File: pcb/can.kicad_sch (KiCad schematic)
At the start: 27 parts, among them J3 C-OBD-II-16M, J4 GND_Connect, U6 TCAN337, U7 LM2842X, U8 LM66100DCK

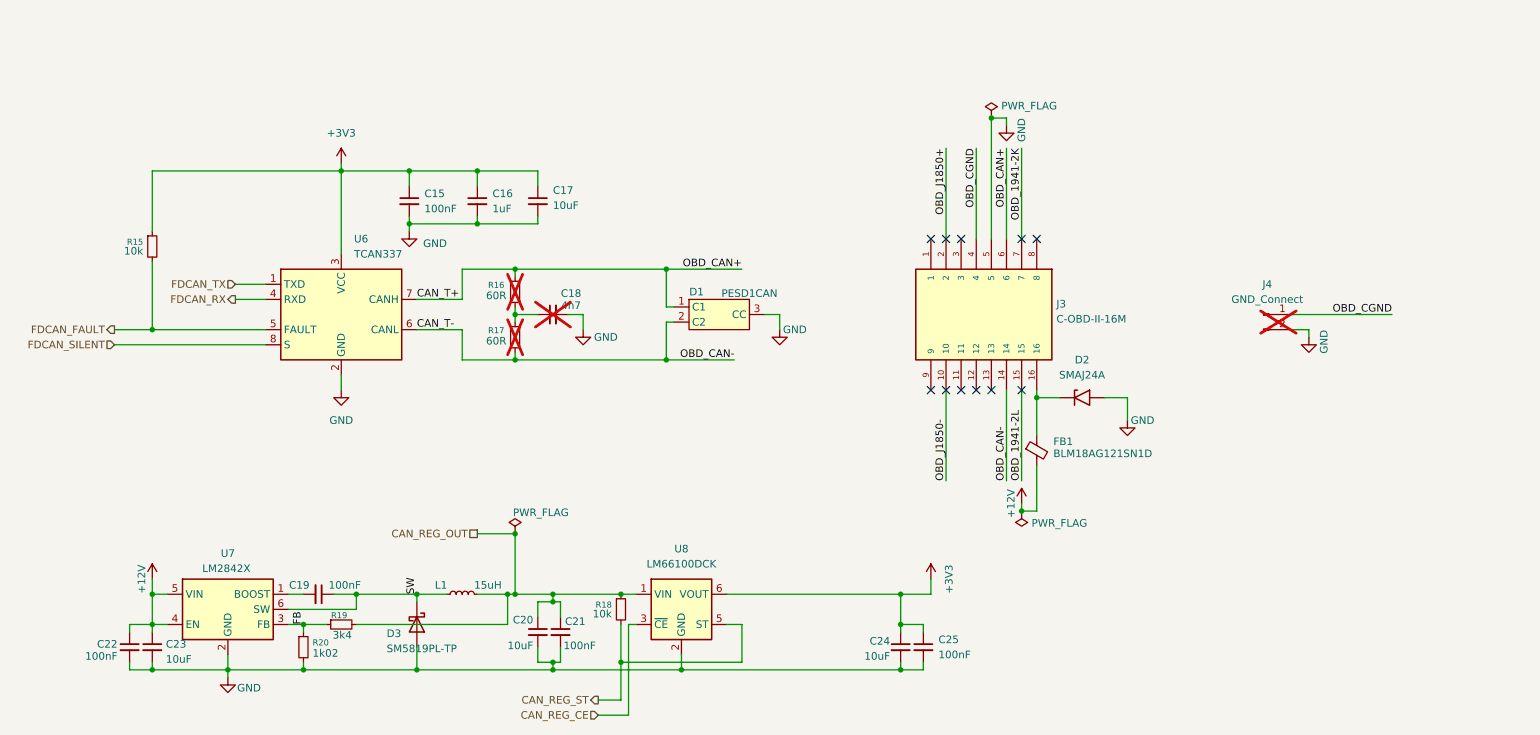
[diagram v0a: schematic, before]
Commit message: add slot for filter
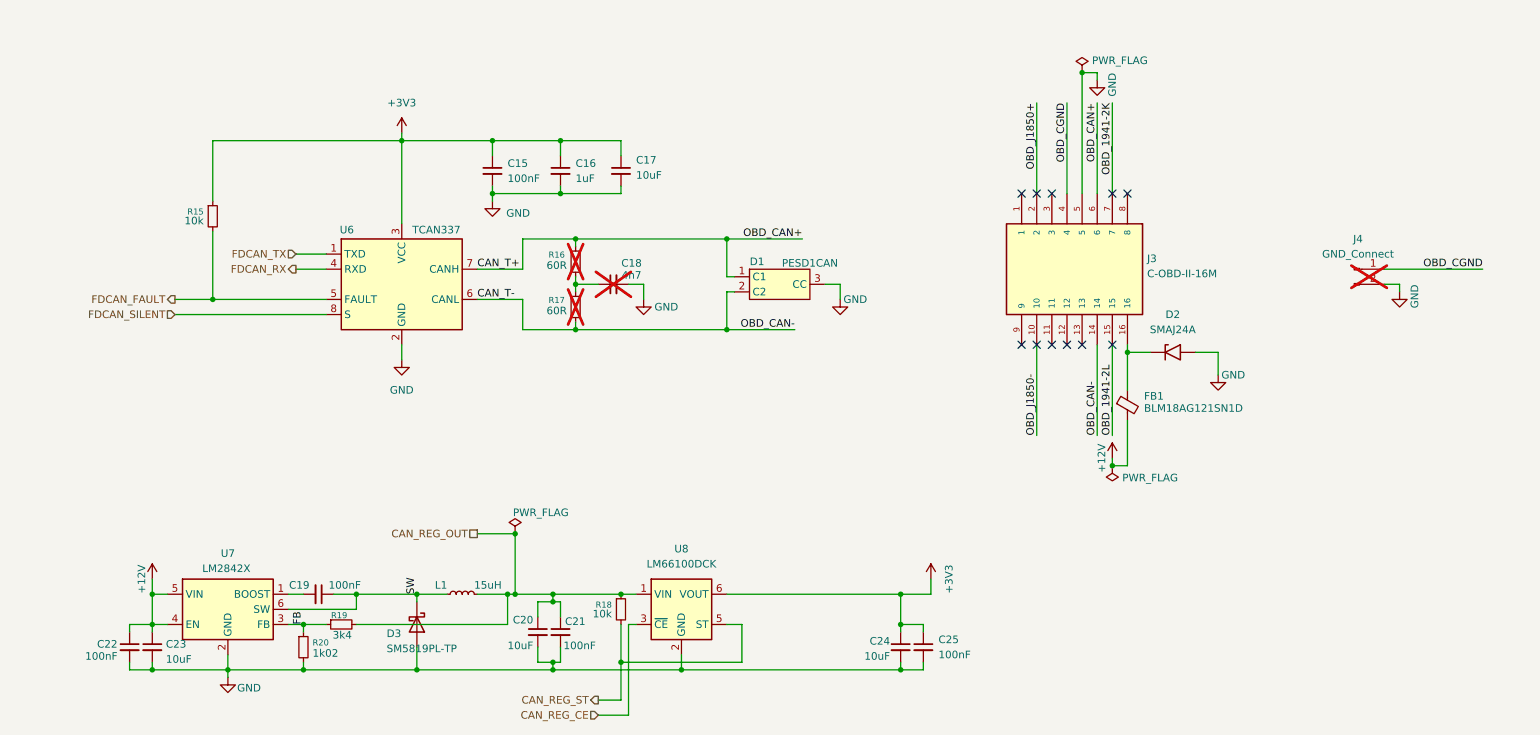
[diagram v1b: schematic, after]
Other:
- moved on the sheet: C15, C16, C17, C18, D1, D2, FB1, J3, J4, R15, R16, R17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

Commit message: update
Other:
- moved on the sheet: C15, C16, C17, C18, C19, C20, C21, C22, C23, C24, C25, D1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
